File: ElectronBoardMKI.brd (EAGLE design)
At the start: 88 x 200 mm, 38 parts, among them IC1 7805TV, Q1 TN0602N3, Q2 TN0602N3, T2 2N2222, T3 2N2222, T4 2N2222

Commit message: Audio
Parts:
- added C3: 250uf, resistor:E5-8,5
- added C7: 10uf, resistor:E5-8,5
- added C8: 0.05uf, resistor:E5-8,5
- added C9: 1uf, resistor:E5-8,5
- added R19: 10k, resistor:0207/12
- added R21, R22: 10k, pot:CT6
- added U1: LM386N, SparkFun-IC-Amplifiers:DIP08
- moved SPEAKER 14.5 mm to (17.5, 141.9)
- moved C1 0.64 mm to (57.8, 125.7)
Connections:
- new net N$1: R21.S, U1.2
- new net N$2: C9.+, U1.7
- new net N$4: R22.A, U1.1
- new net N$5: C7.-, U1.8
- new net N$6: C3.+, C8.+, U1.5
- new net N$7: C8.-, R19.2
- new net N$9: C7.+, R22.S
- new net SPEAKER-OUTPUT: C3.-, SPEAKER.1
- net GND: now also C9.-, R19.1, R21.A, U1.3, U1.4
- net SOUND: now also R21.E; no longer SPEAKER.1
- net VIN: now also U1.6
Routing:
- net N$6: track 0.00 -> 36.7 mm
- net N$4: track 0.00 -> 27.6 mm
- net N$9: track 0.00 -> 15.6 mm
- net N$5: track 0.00 -> 14.8 mm
- net 3V3: track 328.3 -> 316.1 mm
- net N$1: track 0.00 -> 10.8 mm
- net SPEAKER-OUTPUT: track 0.00 -> 10.1 mm
- net VIN: track 167.2 -> 177.0 mm
- net SOUND: track 18.8 -> 27.7 mm, vias 0 -> 1
- net N$2: track 0.00 -> 8.71 mm
- net N$7: track 0.00 -> 8.30 mm

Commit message: Respacing
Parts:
- moved R22 27.9 mm to (57.6, 149.7), turned to 90 degrees
- moved J1 24.6 mm to (13.0, 91.4), turned to 270 degrees
- moved C7 21.4 mm to (67.9, 153.5)
- moved C3 21.3 mm to (22.7, 155.6)
- moved R21 17.4 mm to (57.8, 141.3)
- moved U1 11.6 mm to (68.3, 141.1)
- moved C8 11.2 mm to (78.9, 137.3)
- moved C9 10.7 mm to (77.6, 151.0)
- moved R19 9.10 mm to (85.2, 143.7)
- moved OUT-TEMP 4.44 mm to (12.1, 101.6)
- moved IN-TEMP 4.13 mm to (11.7, 114.3)
- moved SPEAKER 0.64 mm to (17.5, 141.3), turned to 270 degrees
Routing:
- net KEYPAD-A: track 42.5 -> 13.1 mm
- net KEYPAD-B: track 37.4 -> 13.3 mm
- net N$6: track 36.7 -> 60.1 mm
- net SOUND: track 27.7 -> 48.3 mm
- net KEYPAD-1: track 32.8 -> 13.1 mm
- net N$4: track 27.6 -> 11.5 mm
- net KEYPAD-2: track 28.7 -> 13.3 mm
- net KEYPAD-3: track 24.1 -> 13.1 mm
- net N$9: track 15.6 -> 6.82 mm
- net 3V3: track 316.1 -> 308.2 mm
- net N$1: track 10.8 -> 4.27 mm
- net VIN: track 177.0 -> 182.7 mm
- net N$5: track 14.8 -> 9.23 mm
- net KEYPAD-D: track 18.7 -> 14.1 mm
- net N$7: track 8.30 -> 3.81 mm
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
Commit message: Updated Parts
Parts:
- added RX_______TX: (no value), SparkFun-Connectors:1X02_LOCK_LONGPADS
- C3: value 250uf -> 220uf
- C8: value 0.05uf -> 0.047uf; device resistor:E5-8,5 -> resistor:C050-035X075
- Q1, Q2: value TN0602N3 -> BSS170; device transistor-fet:TO-92 -> transistor-fet:TO92
- turned Q1 to 180 degrees
- turned Q2 to 180 degrees
- renumbered SCL__SDA1 to SCL___SDA1, SCL__SDA2 to SCL___SDA2
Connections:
- new net RX: RX_______TX.1, U$1.4
- new net TX: RX_______TX.2, U$1.3
- net N$6: now also C8.1; no longer C8.+
- net N$7: now also C8.2; no longer C8.-
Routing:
- net TX: track 0.00 -> 13.4 mm
- net RX: track 0.00 -> 13.3 mm
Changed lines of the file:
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@@
 <setting verticaltext="up"/>
 </settings>
-<grid distance="0.0125" unitdist="inch" unit="inch" style="lines" multiple="1" display="no" altdistance="5" altunitdist="mil" altunit="mil"/>
+<grid distance="0.000000123031" unitdist="inch" unit="inch" style="lines" multiple="1" display="no" altdistance="5" altunitdist="mil" altunit="mil"/>
 <layers>
 <layer number="1" name="Top" color="4" fill="1" visible="yes" active="yes"/>
@@
 <attribute name="OC_NEWARK" value="69C8588" x="17.4625" y="141.2875" size="1.778" layer="27" rot="R270" display="off"/>
 </element>
-<element name="SCL__SDA1" library="SparkFun-Connectors" library_urn="urn:adsk.eagle:library:513" package="1X02_LOCK_LONGPADS" package3d_urn="urn:adsk.eagle:package:38047/1" value="" x="80.01" y="101.6" rot="R90"/>
-<element name="SCL__SDA2" library="SparkFun-Connectors" library_urn="urn:adsk.eagle:library:513" package="1X02_LOCK_LONGPADS" package3d_urn="urn:adsk.eagle:package:38047/1" value="" x="80.01" y="110.49" rot="R90"/>
+<element name="SCL___SDA1" library="SparkFun-Connectors" library_urn="urn:adsk.eagle:library:513" package="1X02_LOCK_LONGPADS" package3d_urn="urn:adsk.eagle:package:38047/1" value="" x="80.01" y="101.6" rot="R90"/>
+<element name="SCL___SDA2" library="SparkFun-Connectors" library_urn="urn:adsk.eagle:library:513" package="1X02_LOCK_LONGPADS" package3d_urn="urn:adsk.eagle:package:38047/1" value="" x="80.01" y="110.49" rot="R90"/>
 <element name="IN-TEMP" library="SparkFun-Connectors" library_urn="urn:adsk.eagle:library:513" package="1X03_LOCK_LONGPADS" package3d_urn="urn:adsk.eagle:package:38065/1" value="" x="11.7475" y="114.3" rot="R270"/>
 <element name="OUT-TEMP" library="SparkFun-Connectors" library_urn="urn:adsk.eagle:library:513" package="1X03_LOCK_LONGPADS" package3d_urn="urn:adsk.eagle:package:38065/1" value="" x="12.065" y="101.6" rot="R270"/>
@@
 <element name="C1" library="resistor" library_urn="urn:adsk.eagle:library:348" package="E5-8,5" package3d_urn="urn:adsk.eagle:package:25860/1" value="10uf" x="57.785" y="125.73" rot="R270"/>
 <element name="C2" library="resistor" library_urn="urn:adsk.eagle:library:348" package="E5-8,5" package3d_urn="urn:adsk.eagle:package:25860/1" value="1uf" x="80.01" y="125.73" rot="R270"/>
-<element name="Q1" library="transistor-fet" library_urn="urn:adsk.eagle:library:396" package="TO-92" package3d_urn="urn:adsk.eagle:package:28535/2" value="TN0602N3" x="59.69" y="107.95"/>
+<element name="Q1" library="transistor-fet" library_urn="urn:adsk.eagle:library:396" package="TO92" package3d_urn="urn:adsk.eagle:package:28523/2" value="BSS170" x="59.69" y="107.95" rot="R180"/>
 <element name="R12" library="resistor" library_urn="urn:adsk.eagle:library:348" package="0207/12" package3d_urn="urn:adsk.eagle:package:25938/1" value="4.7k" x="49.53" y="111.76" rot="R90"/>
 <element name="R13" library="resistor" library_urn="urn:adsk.eagle:library:348" package="0207/12" package3d_urn="urn:adsk.eagle:package:25938/1" value="4.7k" x="71.12" y="111.76" rot="R90"/>
-<element name="Q2" library="transistor-fet" library_urn="urn:adsk.eagle:library:396" package="TO-92" package3d_urn="urn:adsk.eagle:package:28535/2" value="TN0602N3" x="59.69" y="101.6"/>
+<element name="Q2" library="transistor-fet" library_urn="urn:adsk.eagle:library:396" package="TO92" package3d_urn="urn:adsk.eagle:package:28523/2" value="BSS170" x="59.69" y="101.6" rot="R180"/>
 <element name="R14" library="resistor" library_urn="urn:adsk.eagle:library:348" package="0207/12" package3d_urn="urn:adsk.eagle:package:25938/1" value="4.7k" x="54.61" y="107.95" rot="R90"/>
 <element name="R15" library="resistor" library_urn="urn:adsk.eagle:library:348" package="0207/12" package3d_urn="urn:adsk.eagle:package:25938/1" value="4.7k" x="66.04" y="107.95" rot="R90"/>
@@
 </element>
 <element name="C7" library="resistor" library_urn="urn:adsk.eagle:library:348" package="E5-8,5" package3d_urn="urn:adsk.eagle:package:25860/1" value="10uf" x="67.945" y="153.51125"/>
-<element name="C8" library="resistor" library_urn="urn:adsk.eagle:library:348" package="E5-8,5" package3d_urn="urn:adsk.eagle:package:25860/1" value="0.05uf" x="78.89875" y="137.31875"/>
+<element name="C8" library="resistor" library_urn="urn:adsk.eagle:library:348" package="C050-035X075" package3d_urn="urn:adsk.eagle:package:26193/1" value="0.047uf" x="78.89875" y="137.31875"/>
 <element name="C9" library="resistor" library_urn="urn:adsk.eagle:library:348" package="E5-8,5" package3d_urn="urn:adsk.eagle:package:25860/1" value="1uf" x="77.62875" y="150.97125"/>
 <element name="R19" library="resistor" library_urn="urn:adsk.eagle:library:348" package="0207/12" package3d_urn="urn:adsk.eagle:package:25938/1" value="10k" x="85.24875" y="143.66875" rot="R270"/>
-<element name="C3" library="resistor" library_urn="urn:adsk.eagle:library:348" package="E5-8,5" package3d_urn="urn:adsk.eagle:package:25860/1" value="250uf" x="22.70125" y="155.575" rot="R180"/>
+<element name="C3" library="resistor" library_urn="urn:adsk.eagle:library:348" package="E5-8,5" package3d_urn="urn:adsk.eagle:package:25860/1" value="220uf" x="22.70125" y="155.575" rot="R180"/>
+<element name="RX_______TX" library="SparkFun-Connectors" library_urn="urn:adsk.eagle:library:513" package="1X02_LOCK_LONGPADS" package3d_urn="urn:adsk.eagle:package:38047/1" value="" x="11.7475" y="119.0625" rot="R90"/>
 </elements>
 <signals>
@@
 <wire x1="49.53" y1="118.11" x2="53.34" y2="114.3" width="1.27" layer="1"/>
 <wire x1="53.34" y1="114.3" x2="54.61" y2="114.3" width="1.27" layer="1"/>
-<wire x1="54.61" y1="114.3" x2="55.88" y2="114.3" width="1.27" layer="1"/>
-<wire x1="55.88" y1="114.3" x2="59.69" y2="109.855" width="1.27" layer="1"/>
-<wire x1="59.69" y1="103.505" x2="59.69" y2="109.855" width="0.635" layer="1"/>
-<wire x1="58.26125" y1="94.13875" x2="58.26125" y2="97.8056875" width="0.635" layer="1"/>
-<wire x1="59.6392" y1="109.8042" x2="59.69" y2="109.855" width="0.8128" layer="1"/>
-<wire x1="58.26125" y1="97.8056875" x2="59.6519" y2="99.1963375" width="0.635" layer="1"/>
+<wire x1="55.88" y1="114.3" x2="54.61" y2="114.3" width="0.635" layer="1"/>
+<wire x1="58.26125" y1="94.13875" x2="58.26125" y2="97.8056875" width="1.27" layer="1"/>
+<wire x1="58.26125" y1="97.8056875" x2="59.6519" y2="99.1963375" width="1.27" layer="1"/>
 <wire x1="58.42" y1="93.98" x2="58.42" y2="91.44" width="1.27" layer="1"/>
 <wire x1="8.5725" y1="109.855" x2="8.5725" y2="123.5075" width="1.27" layer="16"/>
@@
 <wire x1="85.324" y1="81.046" x2="85.324" y2="65.004" width="1.27" layer="1"/>
 <wire x1="81.28" y1="82.55" x2="83.82" y2="82.55" width="1.27" layer="1"/>
-<wire x1="59.6519" y1="99.1963375" x2="59.6519" y2="103.380275" width="0.635" layer="1"/>
 <wire x1="58.42" y1="93.98" x2="58.26125" y2="94.13875" width="1.27" layer="1"/>
 <wire x1="28.575" y1="124.46" x2="41.91" y2="124.46" width="1.27" layer="16"/>
 <wire x1="8.5725" y1="97.79" x2="9.8425" y2="96.52" width="1.27" layer="1"/>
 <wire x1="12.065" y1="96.52" x2="9.8425" y2="96.52" width="1.27" layer="1"/>
+<wire x1="59.69" y1="99.695" x2="59.69" y2="106.045" width="0.635" layer="1"/>
+<wire x1="59.69" y1="106.045" x2="59.69" y2="110.49" width="0.635" layer="1"/>
+<wire x1="59.69" y1="110.49" x2="55.88" y2="114.3" width="0.635" layer="1"/>
 </signal>
 <signal name="SCL-3V3">
@@
 </signal>
 <signal name="SCL-5V">
-<contactref element="SCL__SDA1" pad="2"/>
-<contactref element="SCL__SDA2" pad="2"/>
+<contactref element="SCL___SDA1" pad="2"/>
+<contactref element="SCL___SDA2" pad="2"/>
 <contactref element="Q1" pad="3"/>
 <contactref element="R13" pad="1"/>
@@
 </signal>
 <signal name="SDA-5V">
-<contactref element="SCL__SDA1" pad="1"/>
-<contactref element="SCL__SDA2" pad="1"/>
+<contactref element="SCL___SDA1" pad="1"/>
+<contactref element="SCL___SDA2" pad="1"/>
 <contactref element="Q2" pad="3"/>
 <contactref element="R15" pad="1"/>
@@
 <signal name="N$6">
 <contactref element="U1" pad="5"/>
-<contactref element="C8" pad="+"/>
+<contactref element="C8" pad="1"/>
 <contactref element="C3" pad="+"/>
 <wire x1="72.0725" y1="137.31875" x2="76.35875" y2="137.31875" width="1.27" layer="1"/>
@@
 <signal name="N$7">
 <contactref element="R19" pad="2"/>
-<contactref element="C8" pad="-"/>
+<contactref element="C8" pad="2"/>
 <wire x1="81.43875" y1="137.31875" x2="85.24875" y2="137.31875" width="1.27" layer="1"/>
 </signal>
@@
 <wire x1="13.0175" y1="138.7475" x2="21.9075" y2="138.7475" width="0" layer="19" extent="1-1"/>
 </signal>
+<signal name="RX">
+<contactref element="RX_______TX" pad="1"/>
+<contactref element="U$1" pad="4"/>
+<wire x1="24.13" y1="116.84" x2="19.05" y2="116.84" width="0.635" layer="1"/>
+<wire x1="16.9545" y1="118.9355" x2="11.7475" y2="118.9355" width="0.635" layer="1"/>
+<wire x1="19.05" y1="116.84" x2="16.9545" y2="118.9355" width="0.635" layer="1"/>
+</signal>
+<signal name="TX">
+<contactref element="U$1" pad="3"/>
+<contactref element="RX_______TX" pad="2"/>
+<wire x1="20.32" y1="119.38" x2="24.13" y2="119.38" width="0.635" layer="1"/>
+<wire x1="11.7475" y1="121.7295" x2="17.9705" y2="121.7295" width="0.635" layer="1"/>
+<wire x1="17.9705" y1="121.7295" x2="20.32" y2="119.38" width="0.635" layer="1"/>
+</signal>
 </signals>

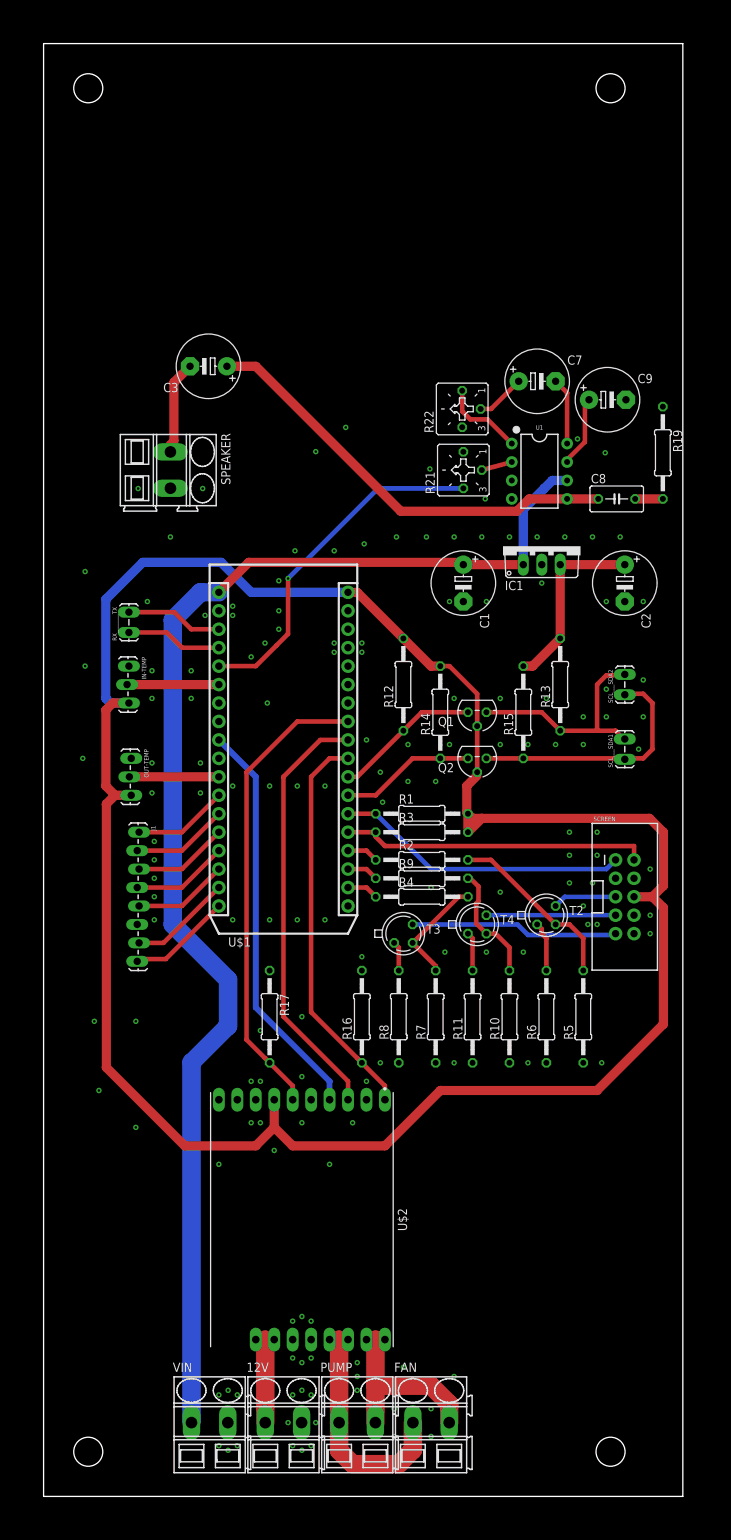
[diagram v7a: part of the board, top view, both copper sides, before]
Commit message: Solid State Relay
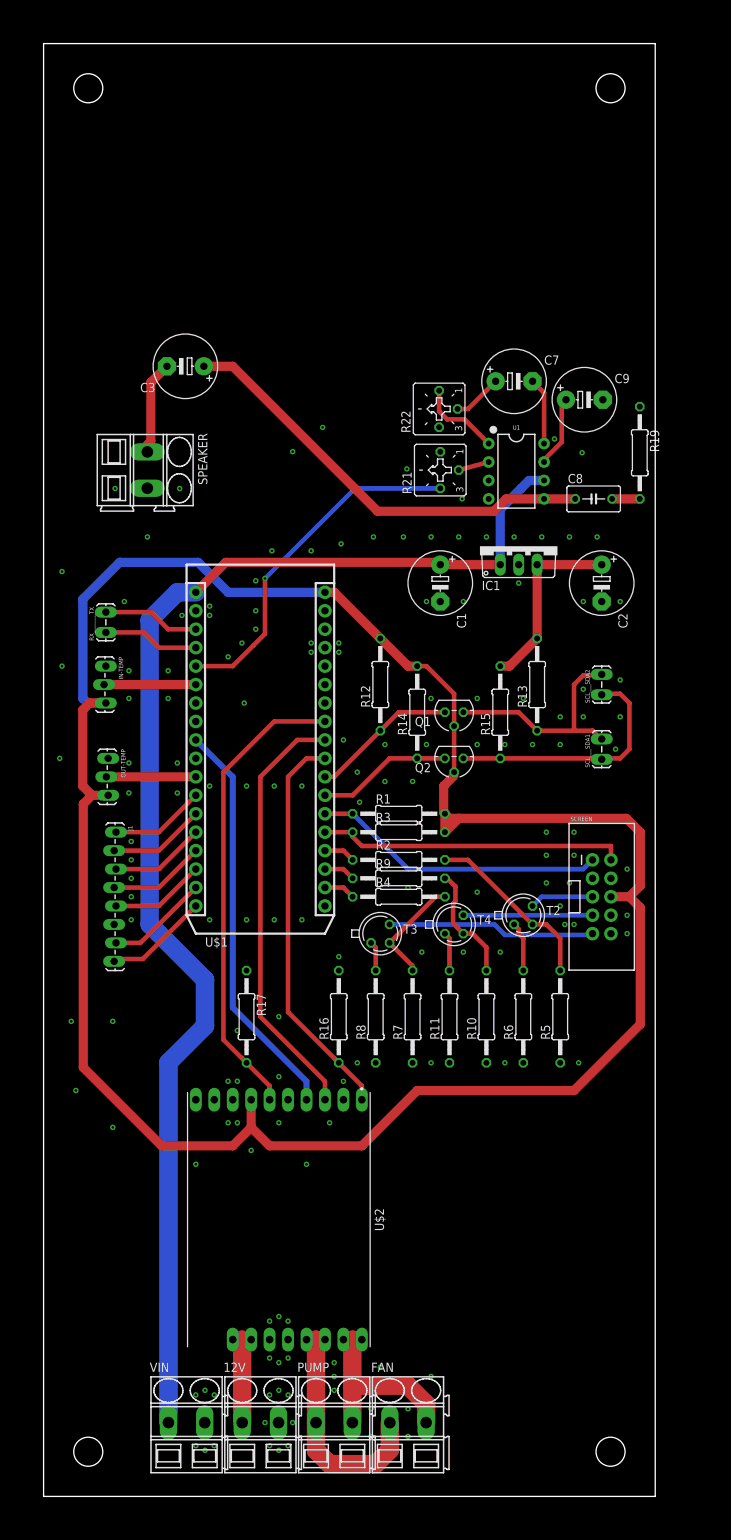
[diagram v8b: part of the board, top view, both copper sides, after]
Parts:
- moved C2 3.18 mm to (76.8, 125.7)
- moved C8 3.18 mm to (75.7, 137.3)
- moved R13 3.18 mm to (67.9, 111.8)
- moved SCL___SDA1 3.18 mm to (76.8, 101.6)
- moved SCL___SDA2 3.18 mm to (76.8, 110.5)
- moved SCREEN 3.18 mm to (76.8, 82.5)
- moved 12V 3.18 mm to (29.8, 10.2)
- moved FAN 3.18 mm to (50.2, 10.2)
- moved R10 3.18 mm to (61.0, 66.0)
- moved R12 3.18 mm to (46.4, 111.8)
- moved R15 3.18 mm to (62.9, 108.0)
- moved R7 3.18 mm to (50.8, 66.0)
- moved R8 3.18 mm to (45.7, 66.0)
- moved T3 3.18 mm to (46.4, 77.5)
- moved U$2 3.18 mm to (32.4, 38.1)
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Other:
- board size 88 x 200 mm -> 84.2 x 200 mm
